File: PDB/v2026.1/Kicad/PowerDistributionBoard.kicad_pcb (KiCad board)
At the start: 2 copper layers, 171 x 112.4 mm, 75 parts, among them J1 12V_EXP3, J10 BMS, J11 IMD, J12 Suspension_Linear_Pot1, J13 Suspension_Linear_Pot2, J14 Suspension_Linear_Pot3, J15 Suspension_Linear_Pot4, J16 CCM_Faults, J17 EXP1_5V, J18 RasPI_5V, J19 LATCH_12V, J2 12V_EXP2, J20 Throttle_Sensor, J21 Current_Sensor, J24 Wheel_Sensor1, J25 Wheel_Sensor2, J26 3V3_EXP, J27 BATTERY_12V, J28 BATTERY_GND, J29 BATTERY_24V, J3 12V_EXP1, J31 FAN1_24V, J32 FAN2_24V, J33 PUMP1_24V, J34 PUMP2_24V, J35 24V_EXP1, J4 RTM, J5 CCM_12V, J7 BSPD, J8 LATCH, J9 TSSI, U1 5to3.3_Linear_Regulator, U2 TLV76150DCYR

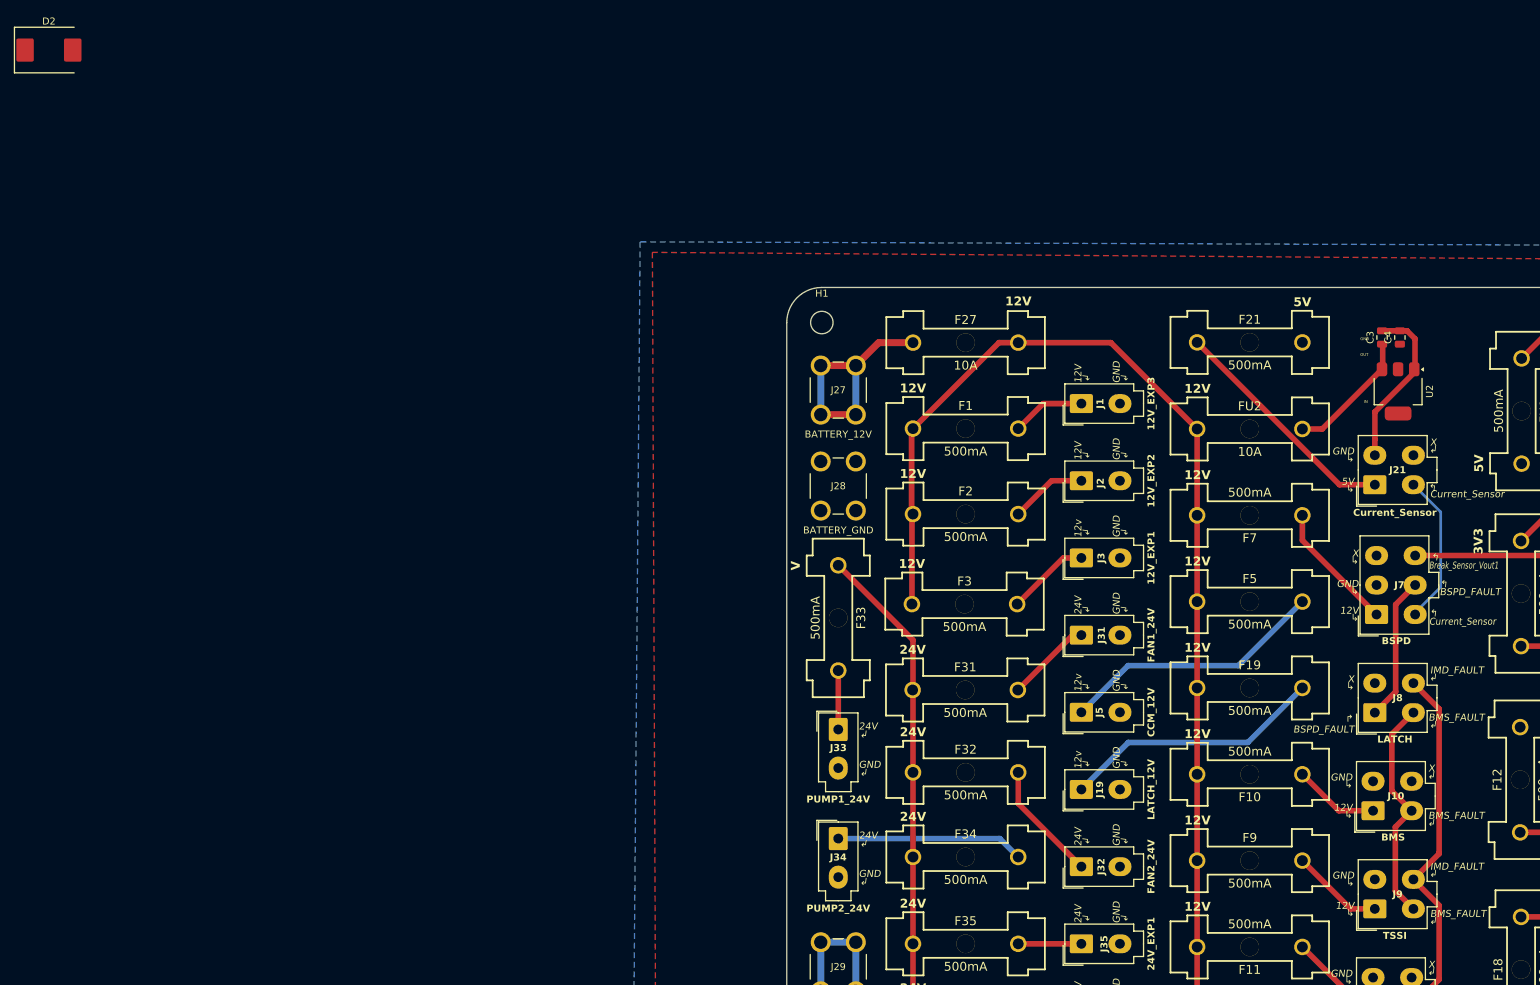
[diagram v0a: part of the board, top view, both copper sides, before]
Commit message: Added 24V line back
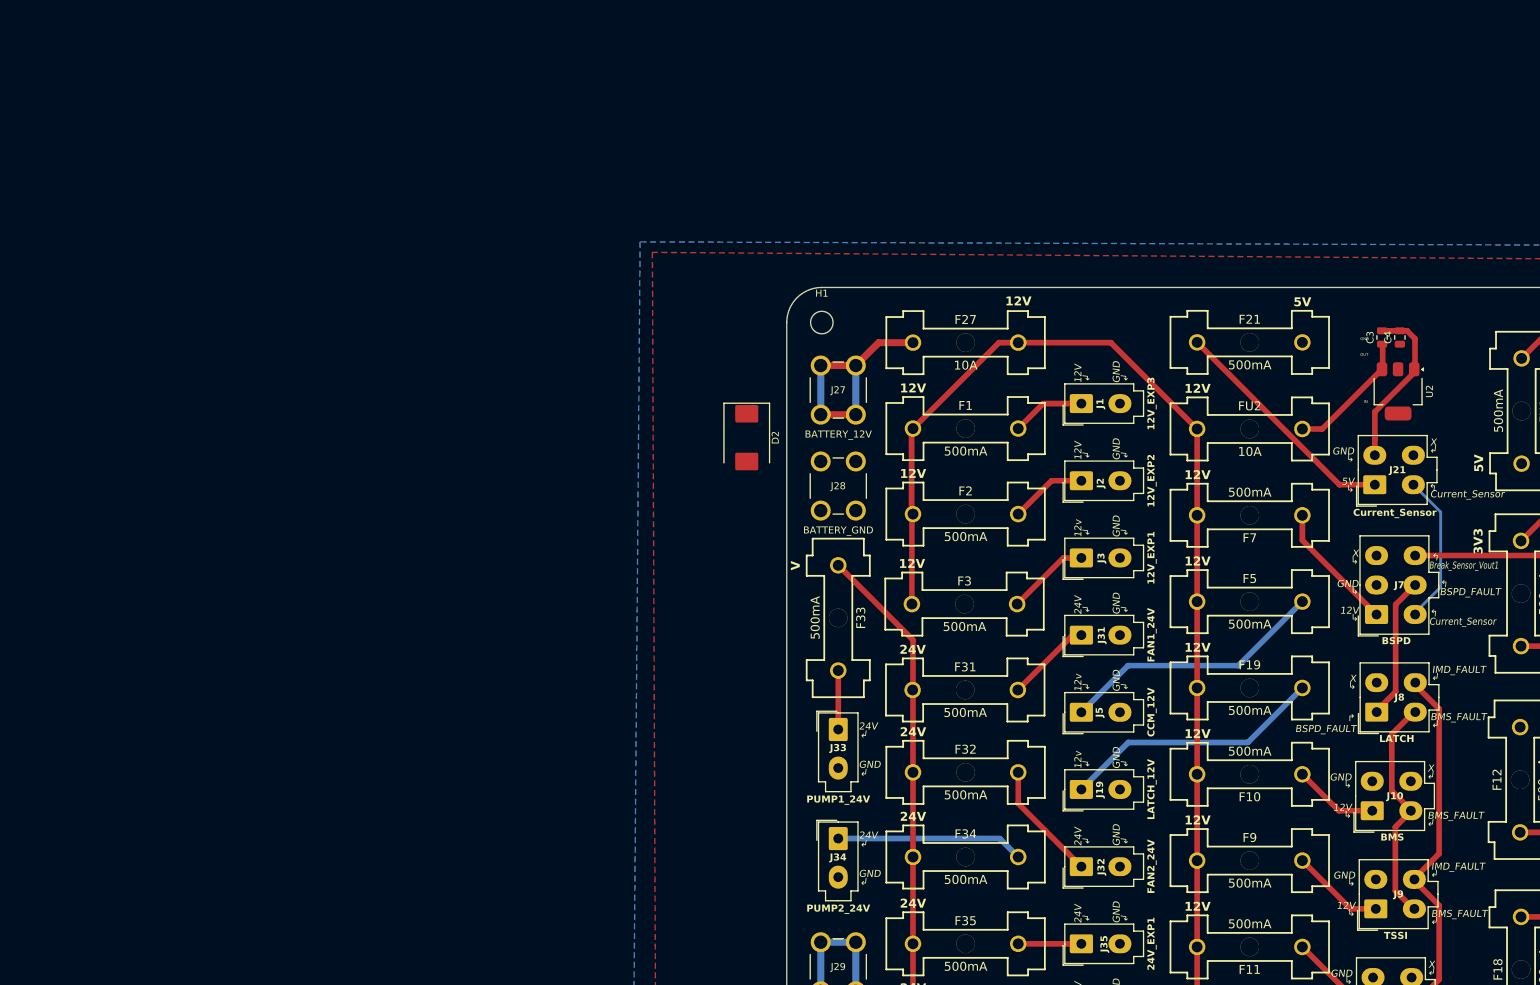
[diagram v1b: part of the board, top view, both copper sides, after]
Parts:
- moved D2 113.8 mm to (44.5, 45.7), turned to -90 degrees
- moved J8 0.28 mm to (134.2, 84.8)
- moved J9 0.14 mm to (134.1, 112.9)
- moved J10 0.11 mm to (133.6, 98.9)

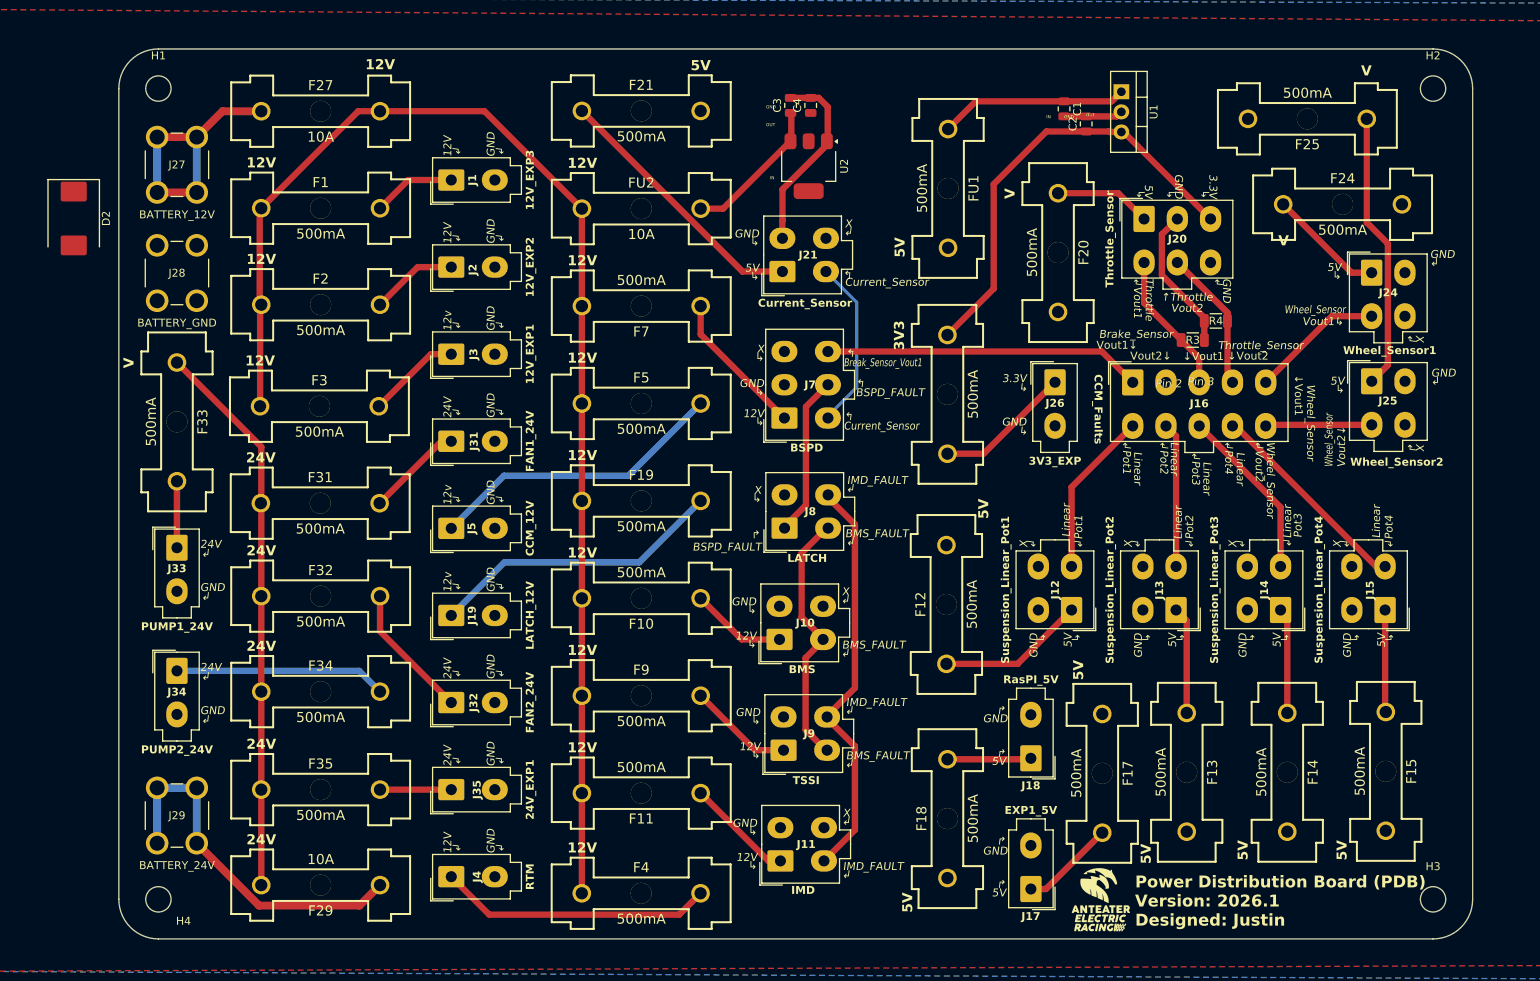
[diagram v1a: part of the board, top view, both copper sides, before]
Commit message: Added plated mounting holes, fixed diode
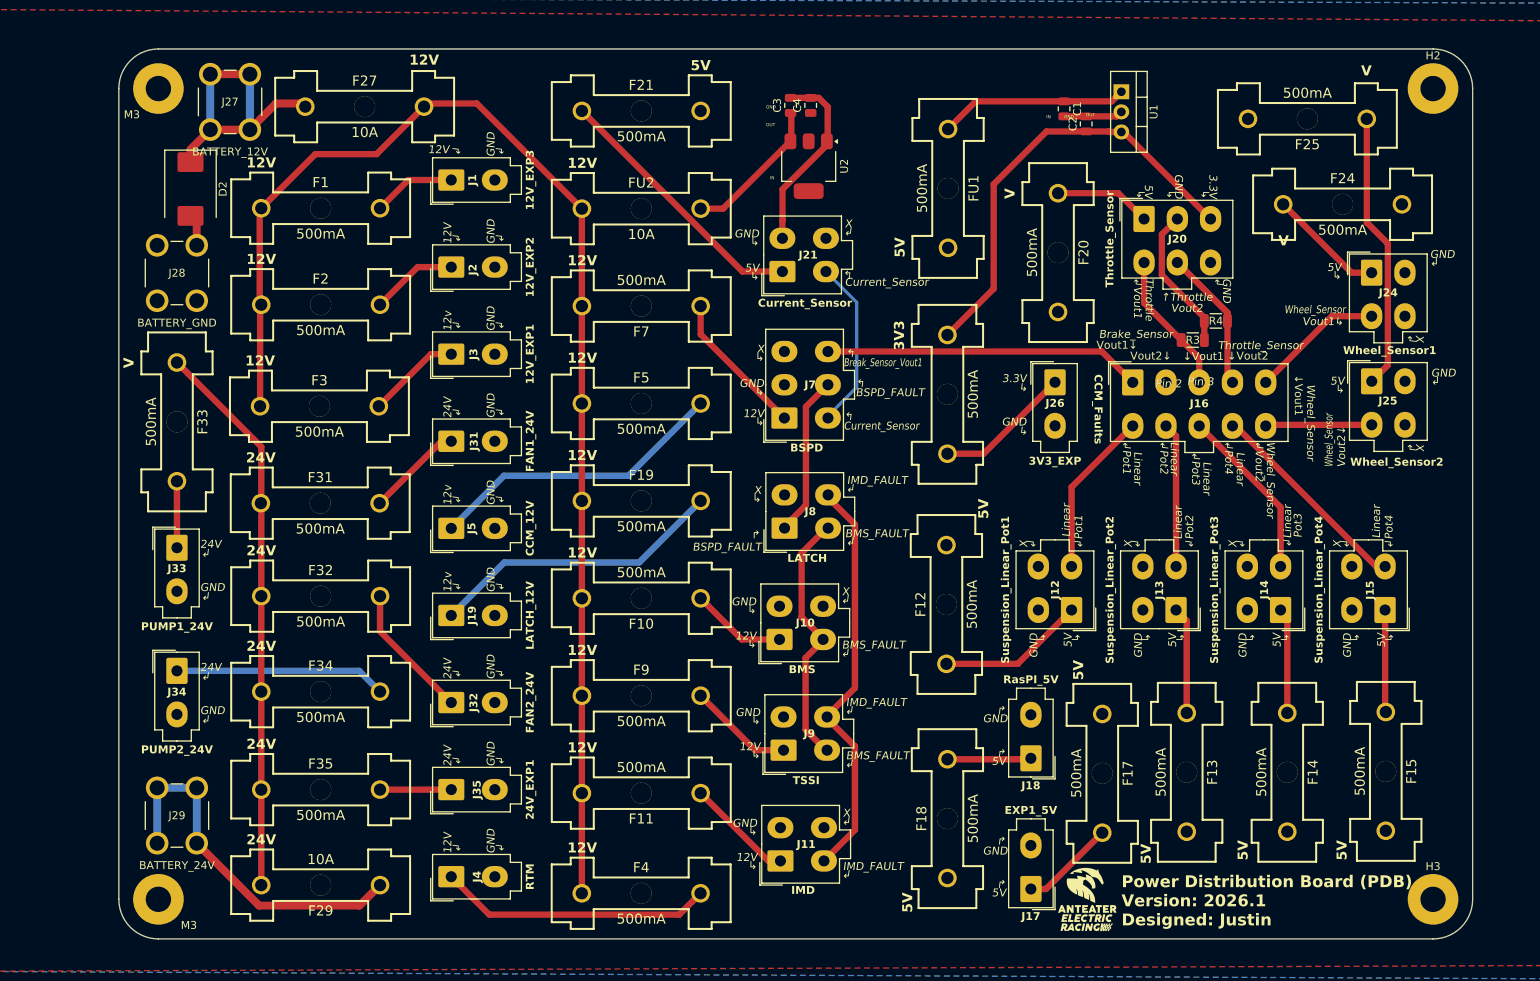
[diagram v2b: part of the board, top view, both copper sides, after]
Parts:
- removed H1, H4: MountingHole M3, MountingHole:MountingHole_3.2mm_M3
- added M3: MountingHole M3, MountingHole:MountingHole_3.2mm_M3_Pad, F.Cu at (55.1, 131.7)
- added M3: MountingHole M3, MountingHole:MountingHole_3.2mm_M3_Pad, F.Cu at (55.1, 29.3)
- H2, H3: footprint MountingHole:MountingHole_3.2mm_M3 -> MountingHole:MountingHole_3.2mm_M3_Pad
- moved D2 15.2 mm to (59.2, 42.0)
- moved J27 10.4 mm to (64.2, 31.0)
- moved F27 5.59 mm to (81.2, 31.6)
- moved REF** 1.71 mm to (172.3, 132.1)
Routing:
- net /Fuse_Batt12V: track 33.5 -> 37.7 mm
- net GND: track 50.2 -> 54.3 mm
- net 12V: track 162.9 -> 163.4 mm

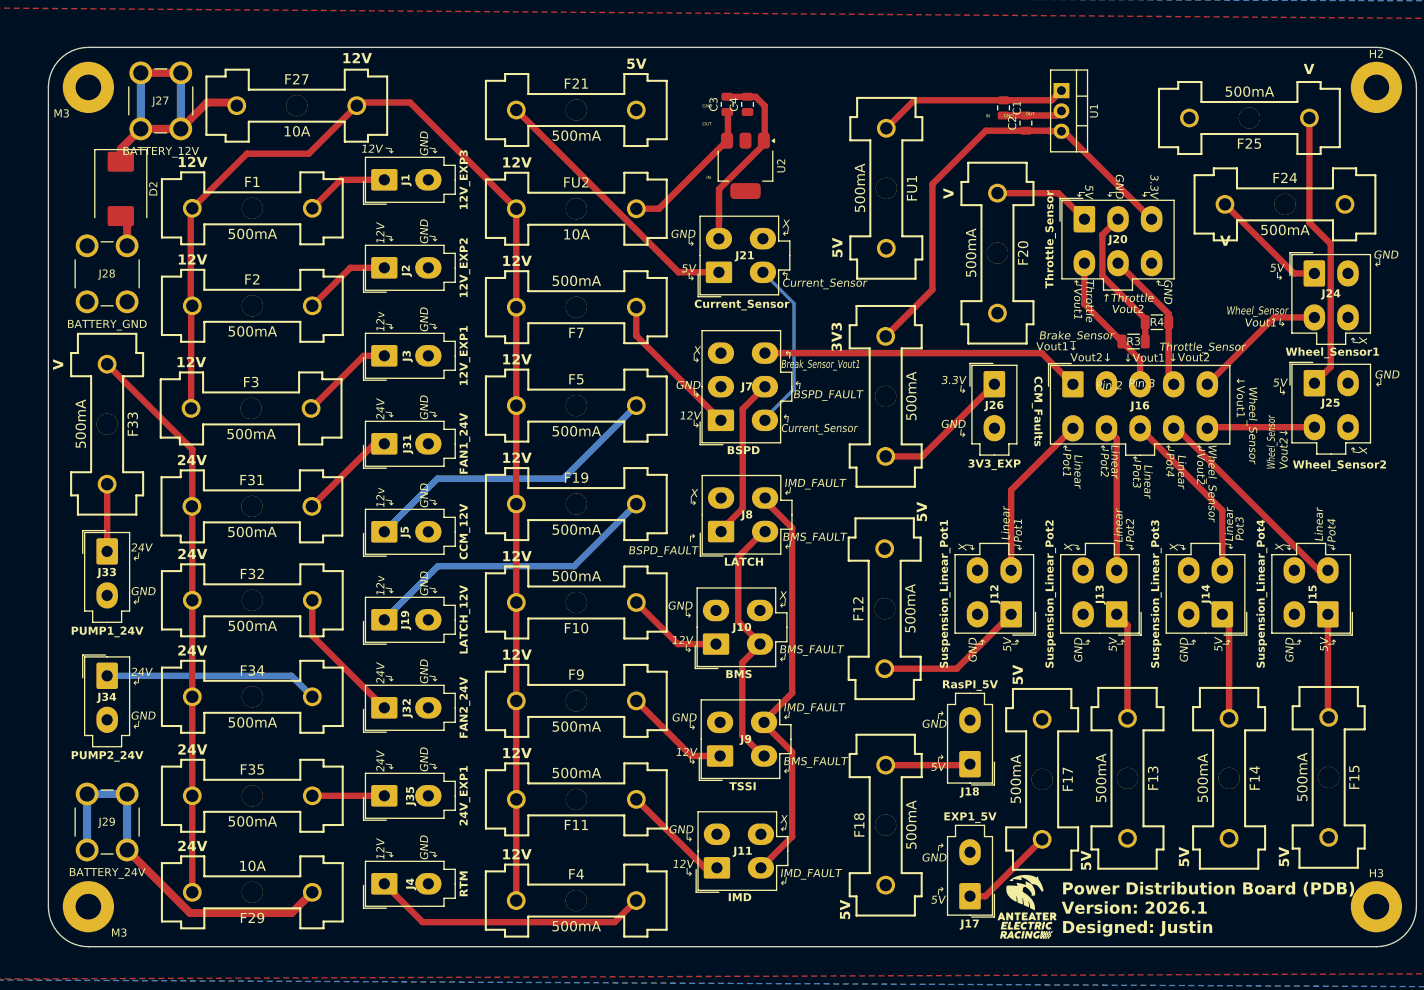
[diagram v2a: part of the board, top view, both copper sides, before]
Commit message: Made quick changes: updated fuse footprint
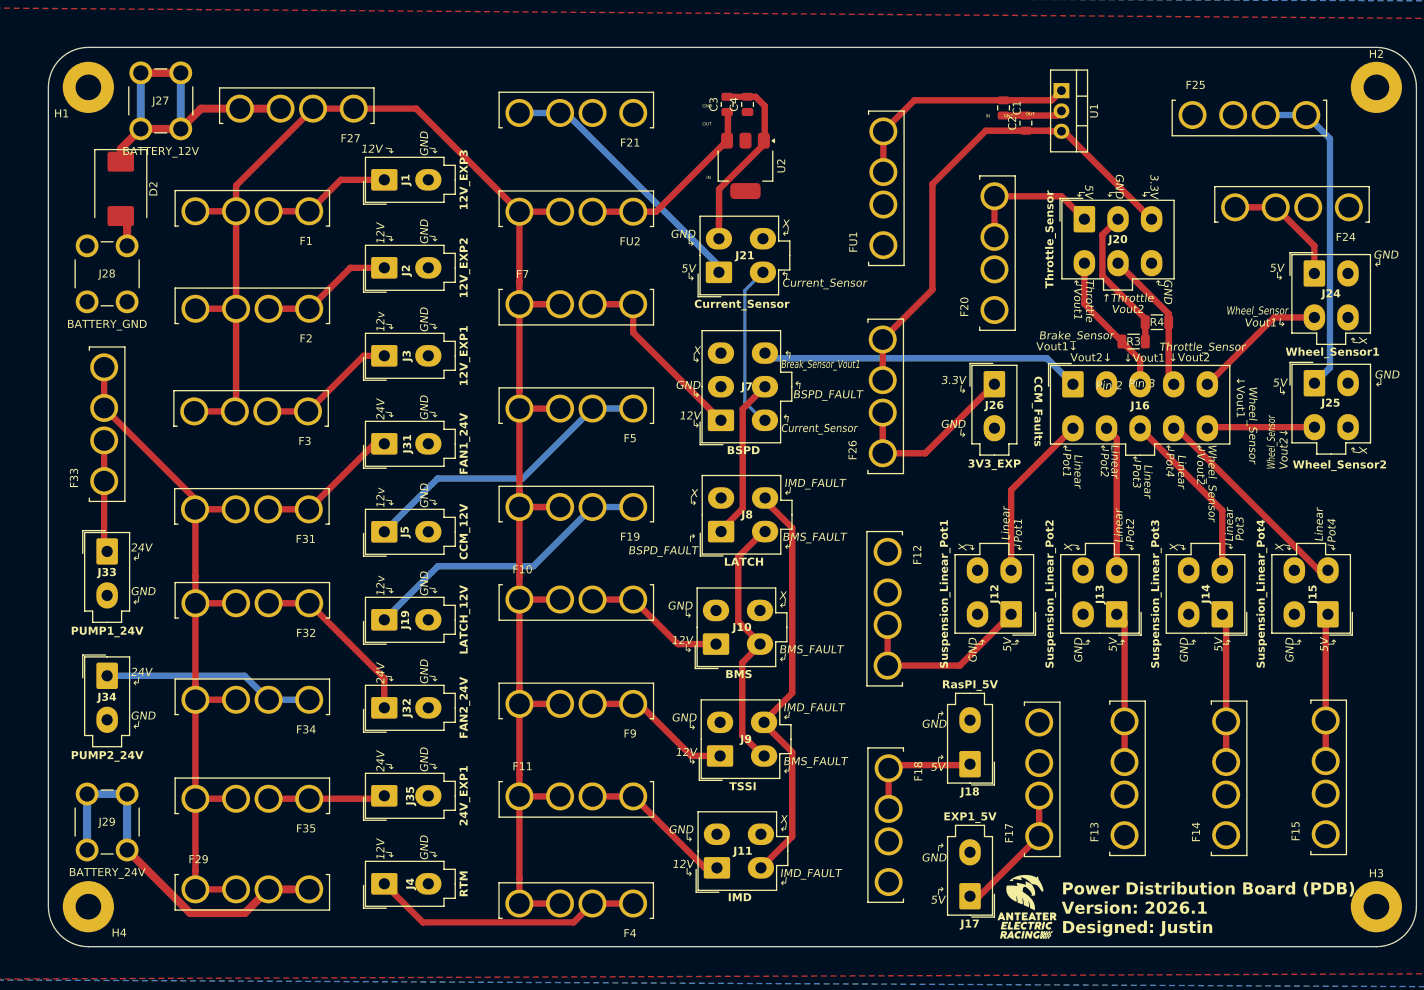
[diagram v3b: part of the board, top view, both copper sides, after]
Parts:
- F1, F10, F11, F12, F13, F14, F15, F17, F18, F19, F2, F20, F21, F24, F25, F26, F27, F29, F3, F31, F32, F33, F34, F35, F4, F5, F7, F9, FU1, FU2: footprint 0footprints:649-SERIES-HOLDER -> 0footprints:FUSE_3522-2
- moved F24 0.88 mm to (205.6, 43.9)
- renumbered M3 to H1, M3 to H4
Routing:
- net 12V: track 163.4 -> 215.4 mm
- net 24V: track 70.5 -> 95.4 mm
- net /Fuse_5to3.3: track 23.9 -> 30.0 mm
- net /Fuse_EXP1_24V: track 9.49 -> 15.2 mm
- net /Fuse_12to5: track 18.5 -> 24.2 mm
- net /Fuse_Pump1: track 8.40 -> 14.0 mm
- net /Fuse_IMD: track 13.6 -> 19.2 mm
- net /Fuse_BMMS: track 12.1 -> 17.7 mm
- net /Fuse_EXP3_12V: track 10.5 -> 16.1 mm
- net /Fuse_EXP2_12V: track 11.0 -> 16.6 mm
- net /Fuse_Fan1: track 12.3 -> 17.9 mm
- net /Fuse_EXP1_12V: track 11.9 -> 17.5 mm
- net 3.3V: track 56.2 -> 61.8 mm
- net /Fuse_BSPD: track 18.5 -> 24.1 mm
- net /Fuse_Lin_Pot4: track 12.9 -> 18.5 mm
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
